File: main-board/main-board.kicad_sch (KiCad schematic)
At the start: 54 parts, among them J4 Conn_01x03_Pin, J5 COM, J6 Conn_01x03_Pin, SW1 SW_SPST, SW2 SW_Push_SPDT, SW3 SW_Push_SPDT, U1 ADA4898-2, U2 ADA4898-2, U3 AD633ANZ

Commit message: Adds Switch footprint and 3d model
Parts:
- SW2, SW3: footprint (none) -> footprints:Switch_Toggle_SPDT_SS12F46
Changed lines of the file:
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@@
       (effects (font (size 1.27 1.27)))
     )
-    (property "Footprint" "" (at 188.595 139.7 0)
+    (property "Footprint" "footprints:Switch_Toggle_SPDT_SS12F46" (at 188.595 139.7 0)
       (effects (font (size 1.27 1.27)) hide)
     )
@@
       (effects (font (size 1.27 1.27)))
     )
-    (property "Footprint" "" (at 187.325 120.65 0)
-      (effects (font (size 1.27 1.27)) hide)
-    )
+    (property "Footprint" "footprints:Switch_Toggle_SPDT_SS12F46" (at 187.325 120.65 0)
+      (effects (font (size 1.27 1.27)) hide)
+    )

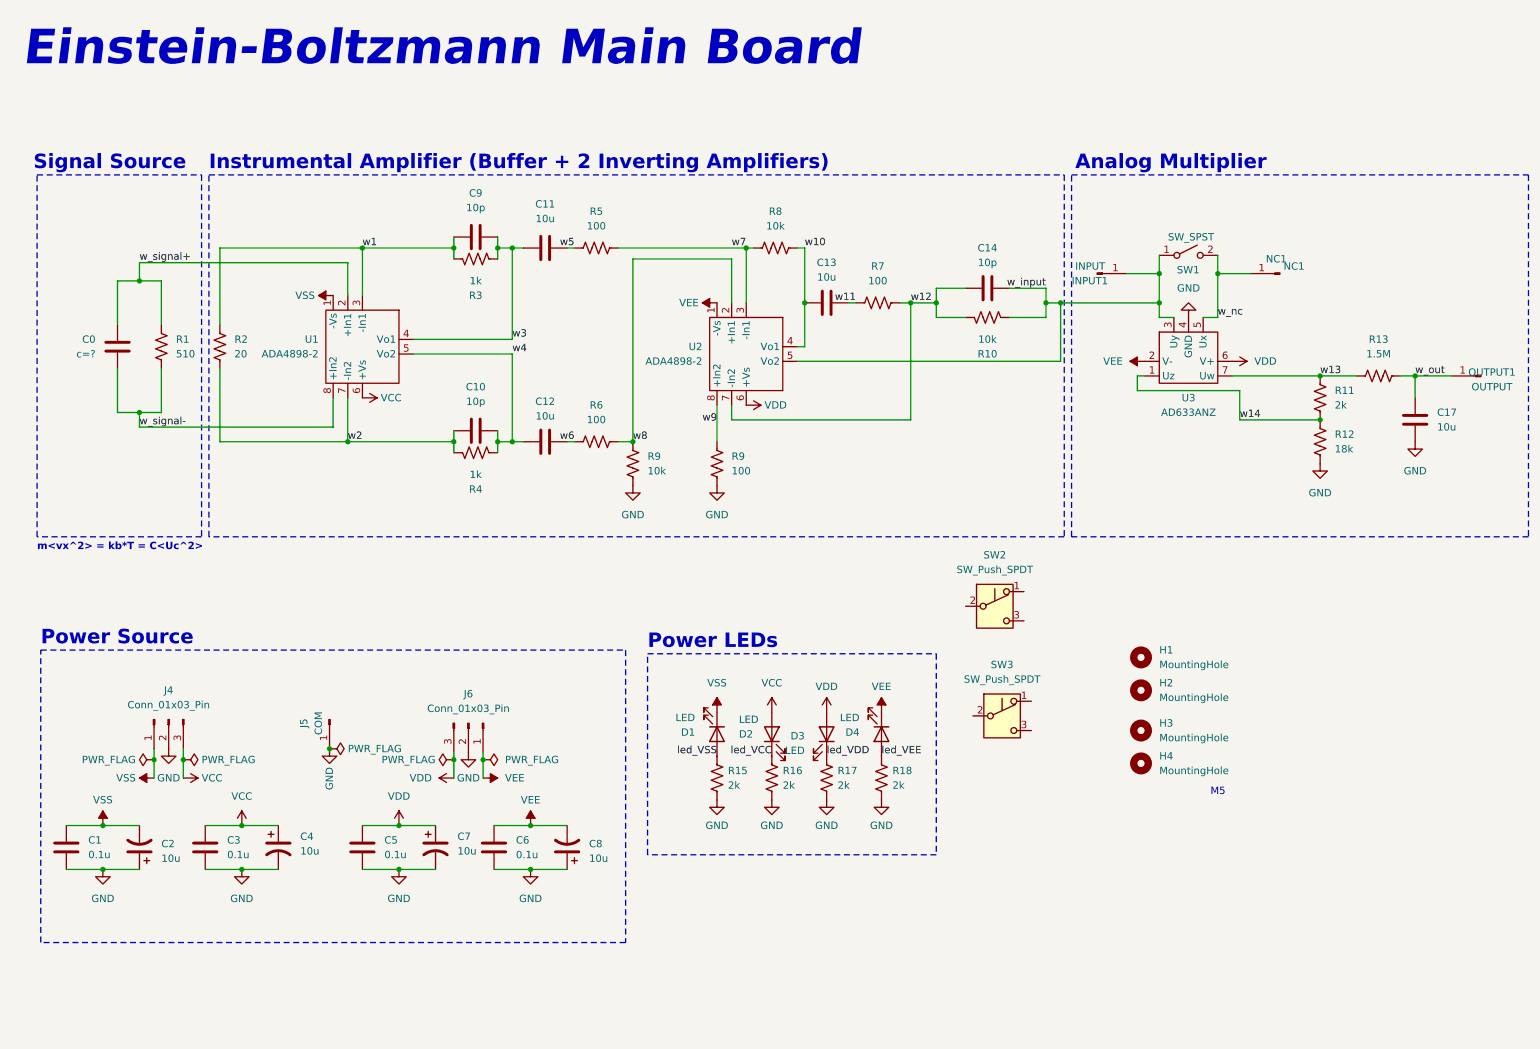
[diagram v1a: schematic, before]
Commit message: Solves the 4 batteries problem
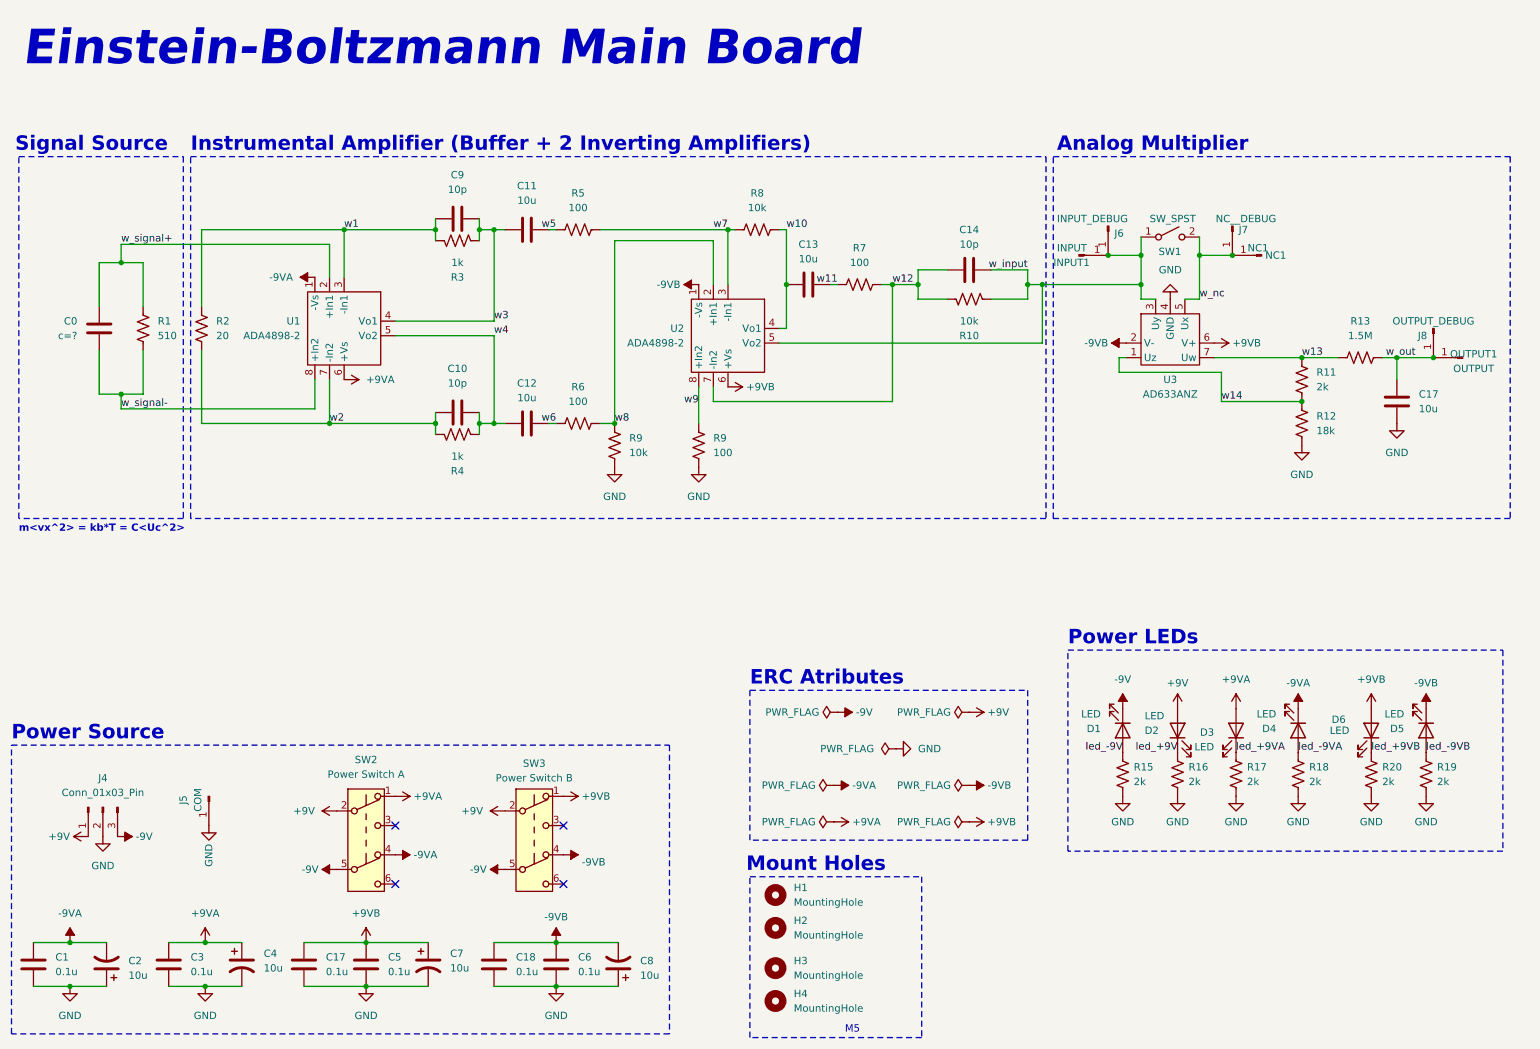
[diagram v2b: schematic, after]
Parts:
- removed J6: Conn_01x03_Pin, footprints:PowerHeader, symbol Connector:Conn_01x03_Pin
- removed SW2, SW3: SW_Push_SPDT, footprints:Switch_Toggle_SPDT_SS12F46, symbol Switch:SW_Push_SPDT
- added C17, C18: 0.1u, Capacitor_THT:C_Disc_D3.0mm_W1.6mm_P2.50mm, symbol Device:C
- added D5, D6: LED, LED_THT:LED_D3.0mm, symbol Device:LED
- added J6: INPUT_DEBUG, Connector_PinHeader_2.54mm:PinHeader_1x01_P2.54mm_Vertical, symbol Connector:Conn_01x01_Pin
- added J7: NC__DEBUG, Connector_PinHeader_2.54mm:PinHeader_1x01_P2.54mm_Vertical, symbol Connector:Conn_01x01_Pin
- added J8: OUTPUT_DEBUG, Connector_PinHeader_2.54mm:PinHeader_1x01_P2.54mm_Vertical, symbol Connector:Conn_01x01_Pin
- added R19, R20: 2k, Resistor_THT:R_Axial_DIN0207_L6.3mm_D2.5mm_P7.62mm_Horizontal, symbol Device:R_US
- added SW2: Power Switch A, Button_Switch_THT:SW_Push_2P2T_Toggle_CK_PVA2xxH4xxxxxxV2, symbol Switch:SW_Push_DPDT
- added SW3: Power Switch B, Button_Switch_THT:SW_Push_2P2T_Toggle_CK_PVA2xxH4xxxxxxV2, symbol Switch:SW_Push_DPDT
- J4: footprint footprints:PowerHeader -> footprints:Banana_Jack_3Pin
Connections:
- net GND: now also C17.2, C18.2, R19.2, R20.2
- net w_input: now also J6.1 (Pin_1)
- net w_nc: now also J7.1 (Pin_1)
- net w_out: now also J8.1 (Pin_1)
- net VCC renamed +9VA
- net +9VA: now also D3.2 (A), SW2.1 (A); no longer D2.2 (A), J4.3 (Pin_3)
- net VDD renamed +9VB
- net +9VB: now also C17.1, D6.2 (A), SW3.1 (A); no longer D3.2 (A)
- net VEE renamed -9VB
- net -9VB: now also C18.1, D5.1 (K), SW3.4 (A); no longer D4.1 (K)
- net VSS renamed -9VA
- net -9VA: now also D4.1 (K), SW2.4 (A); no longer D1.1 (K), J4.1 (Pin_1)
- net led_VCC renamed led_+9V
- net led_VDD renamed led_+9VA
- net led_VEE renamed led_-9VA
- net led_VSS renamed led_-9V
- new net +9V: D2.2 (A), J4.1 (Pin_1), SW2.2 (B), SW3.2 (B)
- new net -9V: D1.1 (K), J4.3 (Pin_3), SW2.5 (B), SW3.5 (B)
- new net led_+9VB: D6.1 (K), R20.1
- new net led_-9VB: D5.2 (A), R19.1
- no-connect marks 0 -> 4
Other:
- note added: "ERC Atributes"
- note added: "Mount Holes"
- moved on the sheet: C0, C1, C10, C11, C12, C13, C14, C17, C2, C3, C4, C5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

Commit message: Save changes
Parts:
- SW2, SW3: footprint Button_Switch_THT:SW_Push_2P2T_Toggle_CK_PVA2xxH4xxxxxxV2 -> footprints:SW_Push_2P2T_Toggle_CK_PSW-8,0R
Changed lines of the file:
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@@
       (effects (font (size 1.27 1.27)))
     )
-    (property "Footprint" "Button_Switch_THT:SW_Push_2P2T_Toggle_CK_PVA2xxH4xxxxxxV2" (at 78.105 156.21 0)
+    (property "Footprint" "footprints:SW_Push_2P2T_Toggle_CK_PSW-8,0R" (at 78.105 156.21 0)
       (effects (font (size 1.27 1.27)) hide)
     )
@@
       (effects (font (size 1.27 1.27)))
     )
-    (property "Footprint" "Button_Switch_THT:SW_Push_2P2T_Toggle_CK_PVA2xxH4xxxxxxV2" (at 107.315 156.21 0)
-      (effects (font (size 1.27 1.27)) hide)
-    )
+    (property "Footprint" "footprints:SW_Push_2P2T_Toggle_CK_PSW-8,0R" (at 107.315 156.21 0)
+      (effects (font (size 1.27 1.27)) hide)
+    )

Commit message: Continues placement process
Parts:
- removed C7, C8: 10u, Capacitor_THT:CP_Radial_D6.3mm_P2.50mm, symbol Device:C_Polarized_US
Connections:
- net +9V: now also C4.1
- net +9VA: no longer C4.1
- net -9V: now also C2.2
- net -9VA: no longer C2.2

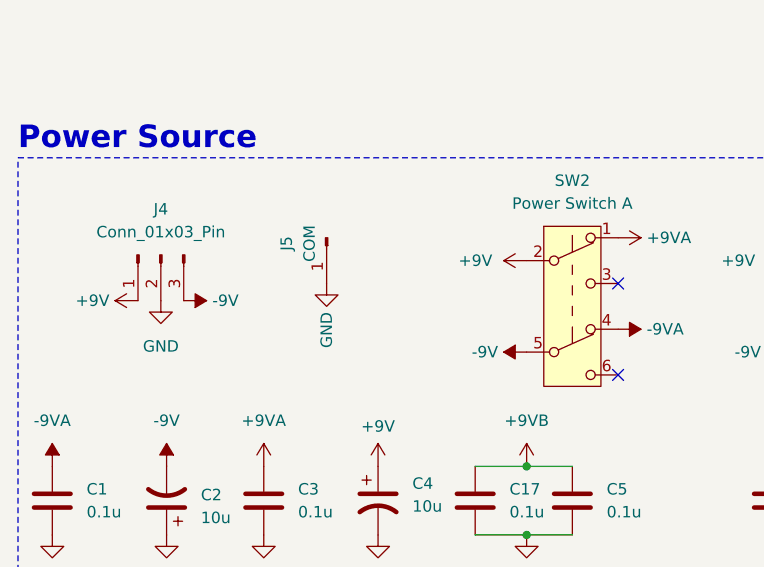
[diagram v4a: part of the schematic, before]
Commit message: Finishes Component displacement
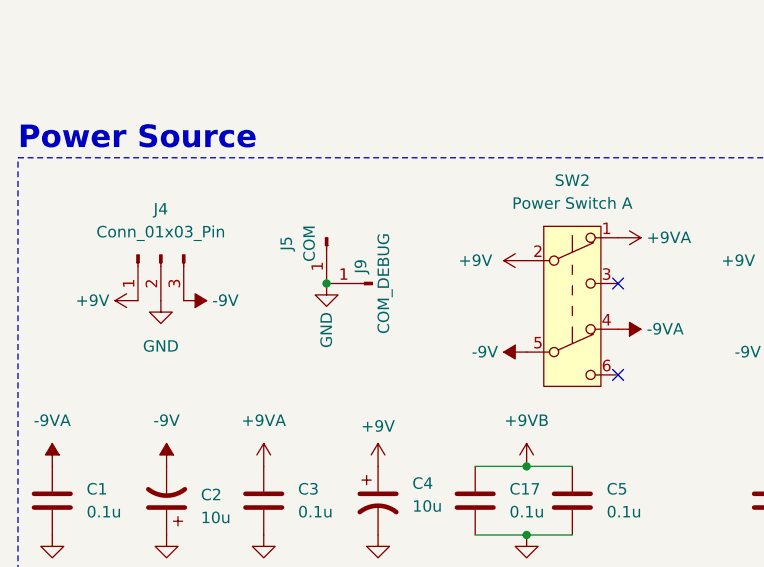
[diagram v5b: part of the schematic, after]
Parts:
- added J9: COM_DEBUG, Connector_PinHeader_2.54mm:PinHeader_1x01_P2.54mm_Vertical, symbol Connector:Conn_01x01_Pin
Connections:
- net GND: now also J9.1 (Pin_1)
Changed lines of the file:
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@@
   (junction (at 106.045 186.69) (diameter 0) (color 0 0 0 0)
+  )
+  (junction (at 50.8 158.75) (diameter 0) (color 0 0 0 0)
   )
   (junction (at 100.33 55.245) (diameter 0) (color 0 0 0 0)
@@
         )
       )
+    )
+  )
+  (symbol (lib_id "Connector:Conn_01x01_Pin") (at 55.88 158.75 180) (unit 1)
+    (in_bom yes) (on_board yes) (dnp no)
+    (property "Reference" "J9" (at 54.61 156.845 90)
+      (effects (font (size 1.27 1.27)))
+    )
+    (property "Value" "COM_DEBUG" (at 57.15 158.75 90)
+      (effects (font (size 1.27 1.27)))
+    )
+    (property "Footprint" "Connector_PinHeader_2.54mm:PinHeader_1x01_P2.54mm_Vertical" (at 55.88 158.75 0)
+      (effects (font (size 1.27 1.27)) hide)
+    )
+    (property "Datasheet" "~" (at 55.88 158.75 0)
+      (effects (font (size 1.27 1.27)) hide)
+    )
+    (property "Sim.Enable" "0" (at 55.88 158.75 0)
+      (effects (font (size 1.27 1.27)) hide)
+    )
+    (pin "1")
+    (instances
+      (project "main-board"
+        (path "/99206265-9bbc-437e-9194-cd0123f9f5d5"
+          (reference "J9") (unit 1)
+        )
+      )

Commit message: Done Routing with DRC 0 Errors and 0 Warnings
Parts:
- D1, D2, D3, D4, D5, D6: footprint LED_THT:LED_D3.0mm -> footprints:LED_D3.0mm
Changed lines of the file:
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@@
     (effects (font (size 2.5 2.5) bold) (justify left bottom))
+  )
+  (label "-9V" (at 160.02 139.065 0) (fields_autoplaced)
+    (effects (font (size 1.27 1.27)) (justify left bottom))
   )
   (label "w_input" (at 193.04 62.23 180) (fields_autoplaced)
@@
     (effects (font (size 1.27 1.27)) (justify left bottom))
   )
+  (label "GND" (at 170.18 145.415 0) (fields_autoplaced)
+    (effects (font (size 1.27 1.27)) (justify left bottom))
+  )
+  (label "+9VB" (at 182.88 158.115 0) (fields_autoplaced)
+    (effects (font (size 1.27 1.27)) (justify left bottom))
+  )
   (label "led_+9VB" (at 252.73 146.05 0) (fields_autoplaced)
     (effects (font (size 1.27 1.27)) (justify left bottom))
@@
     (effects (font (size 1.27 1.27)) (justify left bottom))
   )
+  (label "-9VA" (at 159.385 151.765 0) (fields_autoplaced)
+    (effects (font (size 1.27 1.27)) (justify left bottom))
+  )
   (label "led_+9V" (at 219.075 146.05 180) (fields_autoplaced)
     (effects (font (size 1.27 1.27)) (justify right bottom))
   )
+  (label "+9VA" (at 159.385 158.115 0) (fields_autoplaced)
+    (effects (font (size 1.27 1.27)) (justify left bottom))
+  )
   (label "w6" (at 111.125 88.9 180) (fields_autoplaced)
     (effects (font (size 1.27 1.27)) (justify right bottom))
@@
     (effects (font (size 1.27 1.27)) (justify left bottom))
   )
+  (label "+9V" (at 182.88 139.065 0) (fields_autoplaced)
+    (effects (font (size 1.27 1.27)) (justify left bottom))
+  )
   (label "w10" (at 151.13 55.245 0) (fields_autoplaced)
     (effects (font (size 1.27 1.27)) (justify left bottom))
@@
   (label "w11" (at 160.02 64.77 180) (fields_autoplaced)
     (effects (font (size 1.27 1.27)) (justify right bottom))
+  )
+  (label "-9VB" (at 182.88 151.765 0) (fields_autoplaced)
+    (effects (font (size 1.27 1.27)) (justify left bottom))
   )
   (label "w_signal+" (at 35.56 57.785 0) (fields_autoplaced)
@@
       (effects (font (size 1.27 1.27)) (justify right))
     )
-    (property "Footprint" "LED_THT:LED_D3.0mm" (at 229.235 142.24 0)
+    (property "Footprint" "footprints:LED_D3.0mm" (at 229.235 142.24 0)
       (effects (font (size 1.27 1.27)) hide)
     )
@@
       (effects (font (size 1.27 1.27)) (justify right))
     )
-    (property "Footprint" "LED_THT:LED_D3.0mm" (at 209.55 142.24 0)
+    (property "Footprint" "footprints:LED_D3.0mm" (at 209.55 142.24 0)
       (effects (font (size 1.27 1.27)) hide)
     )
@@
       (effects (font (size 1.27 1.27)) (justify right))
     )
-    (property "Footprint" "LED_THT:LED_D3.0mm" (at 252.73 142.24 0)
+    (property "Footprint" "footprints:LED_D3.0mm" (at 252.73 142.24 0)
       (effects (font (size 1.27 1.27)) hide)
     )
@@
       (effects (font (size 1.27 1.27)) (justify right))
     )
-    (property "Footprint" "LED_THT:LED_D3.0mm" (at 219.075 142.24 0)
+    (property "Footprint" "footprints:LED_D3.0mm" (at 219.075 142.24 0)
       (effects (font (size 1.27 1.27)) hide)
     )
@@
       (effects (font (size 1.27 1.27)) (justify right))
     )
-    (property "Footprint" "LED_THT:LED_D3.0mm" (at 240.03 142.24 0)
+    (property "Footprint" "footprints:LED_D3.0mm" (at 240.03 142.24 0)
       (effects (font (size 1.27 1.27)) hide)
     )
@@
       (effects (font (size 1.27 1.27)) (justify right))
     )
-    (property "Footprint" "LED_THT:LED_D3.0mm" (at 262.255 142.24 0)
-      (effects (font (size 1.27 1.27)) hide)
-    )
+    (property "Footprint" "footprints:LED_D3.0mm" (at 262.255 142.24 0)
+      (effects (font (size 1.27 1.27)) hide)
+    )
